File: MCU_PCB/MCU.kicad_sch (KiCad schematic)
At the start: 6 parts

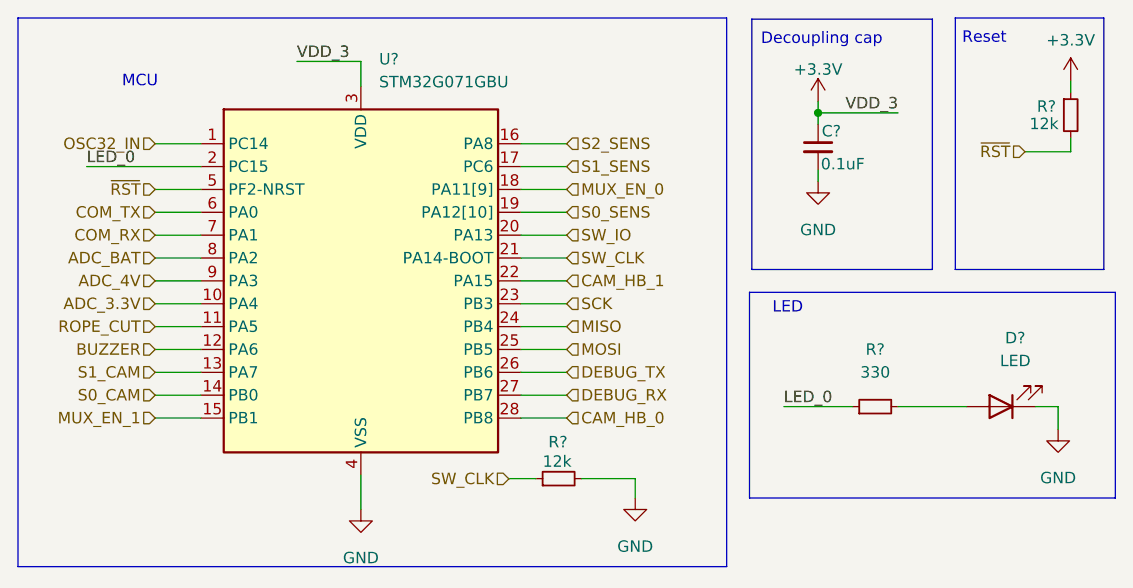
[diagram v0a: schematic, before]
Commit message: 0.1v MCU KiCad
Aesthetics needs to be improved.
Trace width needs to be changed.
More sufficient grounding.
Component placement could be changed.
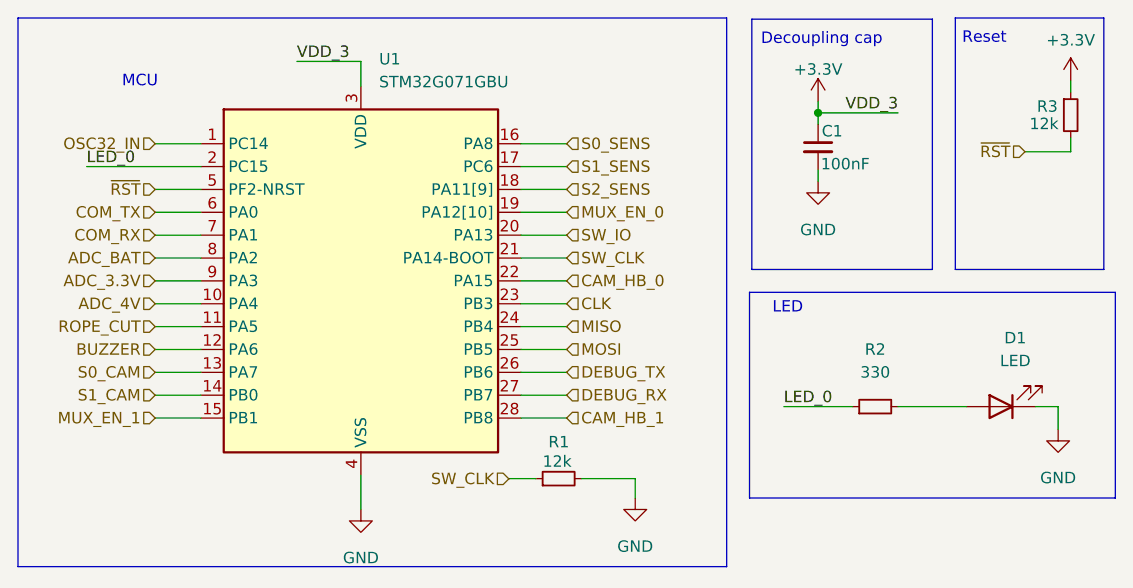
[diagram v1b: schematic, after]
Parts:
- C1: renamed from C?; value 0.1uF -> 100nF; footprint Capacitor_SMD:C_0603_1608Metric -> Capacitor_SMD:C_0402_1005Metric
- D1: renamed from D?; footprint (none) -> LED_SMD:LED_0603_1608Metric
- R1: renamed from R?; footprint Resistor_SMD:R_0603_1608Metric -> Resistor_SMD:R_0402_1005Metric
- R2: renamed from R?; footprint (none) -> Resistor_SMD:R_0402_1005Metric
- R3: renamed from R?; footprint Resistor_SMD:R_0603_1608Metric_Pad0.98x0.95mm_HandSolder -> Resistor_SMD:R_0402_1005Metric
- gave numbers to parts that had none: 1
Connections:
- net ADC_3.3V: now also U1.9 (PA3); no longer U1.10 (PA4)
- net ADC_4V: now also U1.10 (PA4); no longer U1.9 (PA3)
- net CAM_HB_0: now also U1.22 (PA15); no longer U1.28 (PB8)
- net CAM_HB_1: now also U1.28 (PB8); no longer U1.22 (PA15)
- net MUX_EN_0: now also U1.19 (PA12[10]); no longer U1.18 (PA11[9])
- net S0_CAM: now also U1.13 (PA7); no longer U1.14 (PB0)
- net S0_SENS: now also U1.16 (PA8); no longer U1.19 (PA12[10])
- net S1_CAM: now also U1.14 (PB0); no longer U1.13 (PA7)
- net S2_SENS: now also U1.18 (PA11[9]); no longer U1.16 (PA8)
- net SCK renamed CLK
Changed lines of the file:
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@@
     (effects (font (size 1.27 1.27)) (justify left bottom))
   )
-  (hierarchical_label "CAM_HB_1" (shape input) (at 76.2 44.45 0)
+  (hierarchical_label "CAM_HB_1" (shape input) (at 76.2 59.69 0)
     (effects (font (size 1.27 1.27)) (justify left))
   )
@@
     (effects (font (size 1.27 1.27)) (justify right))
   )
-  (hierarchical_label "S2_SENS" (shape input) (at 76.2 29.21 0)
+  (hierarchical_label "S2_SENS" (shape input) (at 76.2 34.29 0)
     (effects (font (size 1.27 1.27)) (justify left))
   )
@@
     (effects (font (size 1.27 1.27)) (justify right))
   )
-  (hierarchical_label "ADC_4V" (shape input) (at 30.48 44.45 180)
+  (hierarchical_label "ADC_4V" (shape input) (at 30.48 46.99 180)
     (effects (font (size 1.27 1.27)) (justify right))
   )
@@
     (effects (font (size 1.27 1.27)) (justify right))
   )
-  (hierarchical_label "ADC_3.3V" (shape input) (at 30.48 46.99 180)
-    (effects (font (size 1.27 1.27)) (justify right))
-  )
-  (hierarchical_label "S1_CAM" (shape input) (at 30.48 54.61 180)
+  (hierarchical_label "ADC_3.3V" (shape input) (at 30.48 44.45 180)
+    (effects (font (size 1.27 1.27)) (justify right))
+  )
+  (hierarchical_label "S1_CAM" (shape input) (at 30.48 57.15 180)
     (effects (font (size 1.27 1.27)) (justify right))
   )
@@
     (effects (font (size 1.27 1.27)) (justify right))
   )
-  (hierarchical_label "CAM_HB_0" (shape input) (at 76.2 59.69 0)
+  (hierarchical_label "CAM_HB_0" (shape input) (at 76.2 44.45 0)
     (effects (font (size 1.27 1.27)) (justify left))
   )
@@
     (effects (font (size 1.27 1.27)) (justify left))
   )
-  (hierarchical_label "MUX_EN_0" (shape input) (at 76.2 34.29 0)
-    (effects (font (size 1.27 1.27)) (justify left))
-  )
-  (hierarchical_label "S0_SENS" (shape input) (at 76.2 36.83 0)
-    (effects (font (size 1.27 1.27)) (justify left))
-  )
-  (hierarchical_label "S0_CAM" (shape input) (at 30.48 57.15 180)
+  (hierarchical_label "MUX_EN_0" (shape input) (at 76.2 36.83 0)
+    (effects (font (size 1.27 1.27)) (justify left))
+  )
+  (hierarchical_label "S0_SENS" (shape input) (at 76.2 29.21 0)
+    (effects (font (size 1.27 1.27)) (justify left))
+  )
+  (hierarchical_label "S0_CAM" (shape input) (at 30.48 54.61 180)
     (effects (font (size 1.27 1.27)) (justify right))
   )
@@
     (effects (font (size 1.27 1.27)) (justify right))
   )
-  (hierarchical_label "SCK" (shape input) (at 76.2 46.99 0)
+  (hierarchical_label "CLK" (shape input) (at 76.2 46.99 0)
     (effects (font (size 1.27 1.27)) (justify left))
   )
@@
   (symbol (lib_id "Device:R_Small") (at 132.207 26.035 0) (unit 1)
     (in_bom yes) (on_board yes)
-    (property "Reference" "R?" (id 0) (at 128.4478 25.0698 0)
+    (property "Reference" "R3" (id 0) (at 128.4478 25.0698 0)
       (effects (font (size 1.27 1.27)) (justify left))
     )
@@
       (effects (font (size 1.27 1.27)) (justify left))
     )
-    (property "Footprint" "Resistor_SMD:R_0603_1608Metric_Pad0.98x0.95mm_HandSolder" (id 2) (at 132.207 26.035 0)
+    (property "Footprint" "Resistor_SMD:R_0402_1005Metric" (id 2) (at 132.207 26.035 0)
       (effects (font (size 1.27 1.27)) hide)
     )
@@
   (symbol (lib_id "Device:C_Small") (at 104.14 29.591 0) (unit 1)
     (in_bom yes) (on_board yes)
-    (property "Reference" "C?" (id 0) (at 104.5464 27.813 0)
-      (effects (font (size 1.27 1.27)) (justify left))
-    )
-    (property "Value" "0.1uF" (id 1) (at 104.4448 31.4706 0)
-      (effects (font (size 1.27 1.27)) (justify left))
-    )
-    (property "Footprint" "Capacitor_SMD:C_0603_1608Metric" (id 2) (at 104.14 29.591 0)
+    (property "Reference" "C1" (id 0) (at 104.5464 27.813 0)
+      (effects (font (size 1.27 1.27)) (justify left))
+    )
+    (property "Value" "100nF" (id 1) (at 104.4448 31.4706 0)
+      (effects (font (size 1.27 1.27)) (justify left))
+    )
+    (property "Footprint" "Capacitor_SMD:C_0402_1005Metric" (id 2) (at 104.14 29.591 0)
       (effects (font (size 1.27 1.27)) hide)
     )
@@
   (symbol (lib_id "power:GND") (at 53.34 69.85 0) (unit 1)
     (in_bom yes) (on_board yes) (fields_autoplaced)
-    (property "Reference" "#PWR?" (id 0) (at 53.34 76.2 0)
+    (property "Reference" "#PWR0107" (id 0) (at 53.34 76.2 0)
       (effects (font (size 1.27 1.27)) hide)
     )
@@
   (symbol (lib_id "power:+3.3V") (at 132.207 22.225 0) (unit 1)
     (in_bom yes) (on_board yes) (fields_autoplaced)
-    (property "Reference" "#PWR?" (id 0) (at 132.207 26.035 0)
+    (property "Reference" "#PWR0105" (id 0) (at 132.207 26.035 0)
       (effects (font (size 1.27 1.27)) hide)
     )
@@
   (symbol (lib_id "schematics:STM32G071GBU") (at 53.34 48.26 0) (unit 1)
     (in_bom yes) (on_board yes) (fields_autoplaced)
-    (property "Reference" "U?" (id 0) (at 55.3594 19.812 0)
+    (property "Reference" "U1" (id 0) (at 55.3594 19.812 0)
       (effects (font (size 1.27 1.27)) (justify left))
     )
@@
   (symbol (lib_id "power:GND") (at 83.82 68.58 0) (unit 1)
     (in_bom yes) (on_board yes) (fields_autoplaced)
-    (property "Reference" "#PWR?" (id 0) (at 83.82 74.93 0)
+    (property "Reference" "#PWR0109" (id 0) (at 83.82 74.93 0)
       (effects (font (size 1.27 1.27)) hide)
     )
@@
   (symbol (lib_id "Device:R_Small") (at 75.311 66.421 90) (unit 1)
     (in_bom yes) (on_board yes)
-    (property "Reference" "R?" (id 0) (at 74.168 62.357 90)
+    (property "Reference" "R1" (id 0) (at 74.168 62.357 90)
       (effects (font (size 1.27 1.27)) (justify right))
     )
@@
       (effects (font (size 1.27 1.27)) (justify right))
     )
-    (property "Footprint" "Resistor_SMD:R_0603_1608Metric" (id 2) (at 75.311 66.421 0)
+    (property "Footprint" "Resistor_SMD:R_0402_1005Metric" (id 2) (at 75.311 66.421 0)
       (effects (font (size 1.27 1.27)) hide)
     )
@@
   (symbol (lib_id "Device:LED") (at 124.46 58.42 180) (unit 1)
     (in_bom yes) (on_board yes) (fields_autoplaced)
-    (property "Reference" "D?" (id 0) (at 126.0475 50.8 0))
+    (property "Reference" "D1" (id 0) (at 126.0475 50.8 0))
     (property "Value" "LED" (id 1) (at 126.0475 53.34 0))
-    (property "Footprint" "" (id 2) (at 124.46 58.42 0)
+    (property "Footprint" "LED_SMD:LED_0603_1608Metric" (id 2) (at 124.46 58.42 0)
       (effects (font (size 1.27 1.27)) hide)
     )
@@
   (symbol (lib_id "Device:R_Small") (at 110.49 58.42 90) (unit 1)
     (in_bom yes) (on_board yes) (fields_autoplaced)
-    (property "Reference" "R?" (id 0) (at 110.49 52.07 90))
+    (property "Reference" "R2" (id 0) (at 110.49 52.07 90))
     (property "Value" "330" (id 1) (at 110.49 54.61 90))
-    (property "Footprint" "" (id 2) (at 110.49 58.42 0)
+    (property "Footprint" "Resistor_SMD:R_0402_1005Metric" (id 2) (at 110.49 58.42 0)
       (effects (font (size 1.27 1.27)) hide)
     )
@@
   (symbol (lib_id "power:GND") (at 104.14 33.401 0) (unit 1)
     (in_bom yes) (on_board yes) (fields_autoplaced)
-    (property "Reference" "#PWR?" (id 0) (at 104.14 39.751 0)
+    (property "Reference" "#PWR0106" (id 0) (at 104.14 39.751 0)
       (effects (font (size 1.27 1.27)) hide)
     )
@@
   (symbol (lib_id "power:GND") (at 130.81 60.96 0) (unit 1)
     (in_bom yes) (on_board yes) (fields_autoplaced)
-    (property "Reference" "#PWR?" (id 0) (at 130.81 67.31 0)
+    (property "Reference" "#PWR0108" (id 0) (at 130.81 67.31 0)
       (effects (font (size 1.27 1.27)) hide)
     )
@@
   (symbol (lib_id "power:+3.3V") (at 104.14 24.511 0) (unit 1)
     (in_bom yes) (on_board yes)
-    (property "Reference" "#PWR?" (id 0) (at 104.14 28.321 0)
-      (effects (font (size 1.27 1.27)) hide)
-    )
+    (property "Reference" "#PWR0104" (id 0) (at 104.14 28.321 0)
+      (effects (font (size 1.27 1.27)) hide)
+    )
